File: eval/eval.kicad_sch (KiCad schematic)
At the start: 5 parts, among them J1 TC2030, U9 STM32G0B1CBTx

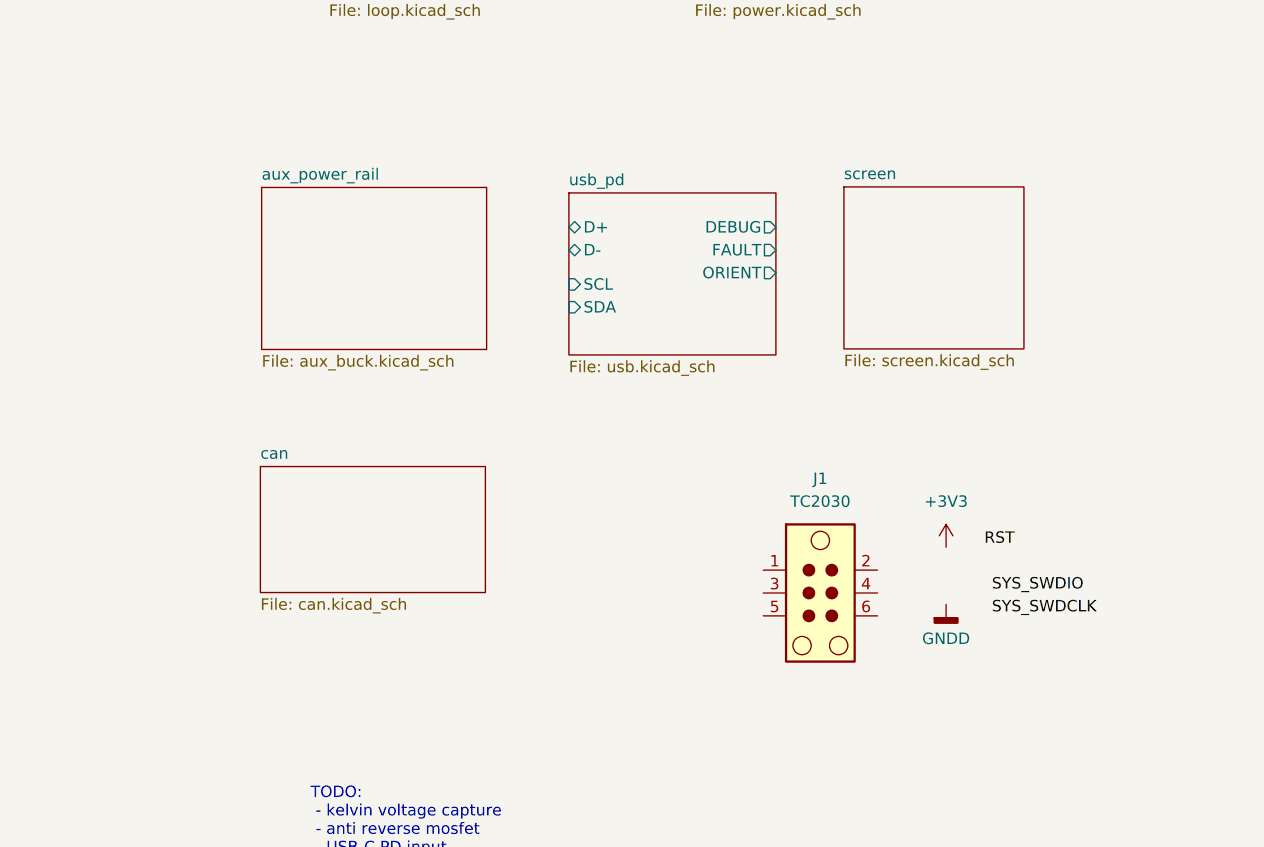
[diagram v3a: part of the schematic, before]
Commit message: add CAN to sch
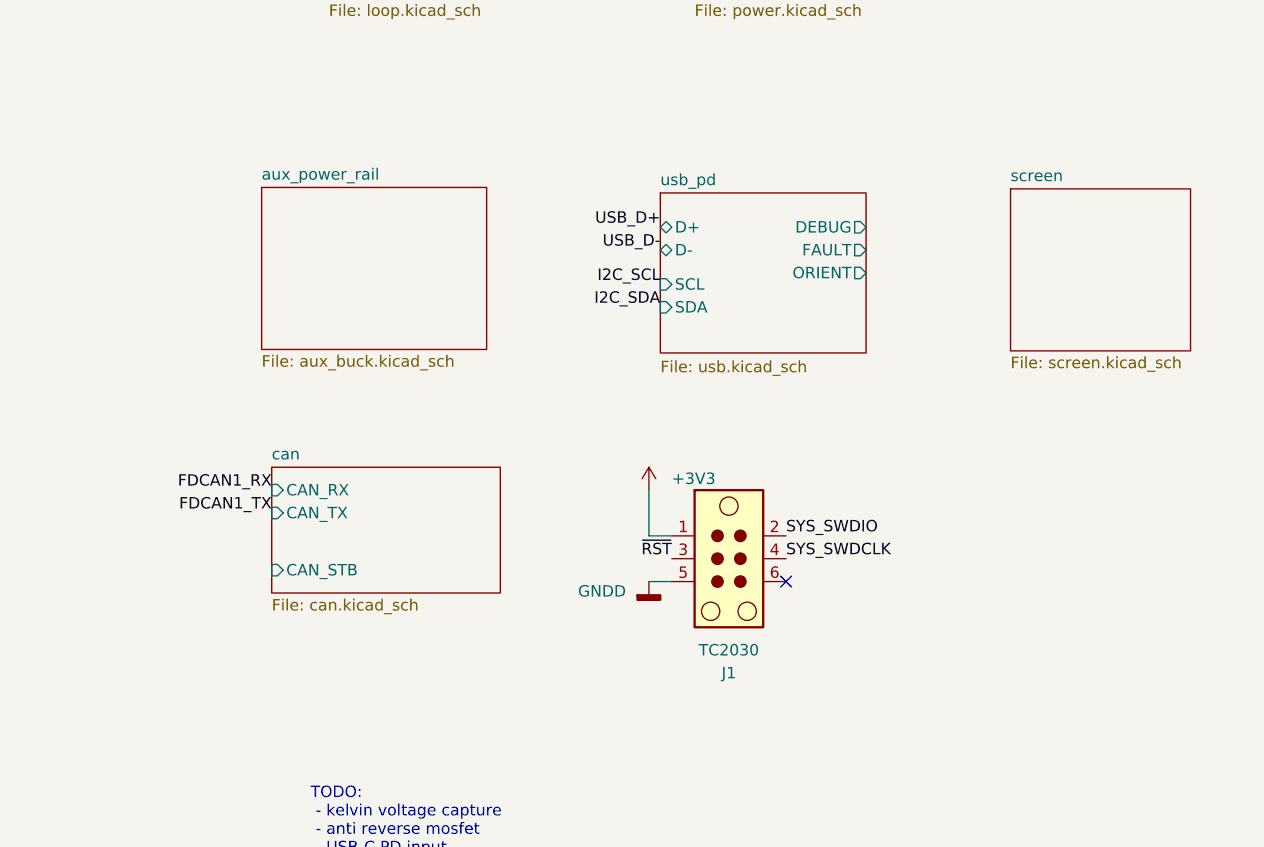
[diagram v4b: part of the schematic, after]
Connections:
- net +3V3: now also J1.1
- net GNDA: now also J1.5
- net SYS_SWDCLK: now also J1.4
- net SYS_SWDIO: now also J1.2
- net ~{RST}: now reaches J1.3
- no-connect marks 0 -> 1
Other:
- sheet can ports: added CAN_RX, CAN_STB, CAN_TX; removed none
- moved on the sheet: J1
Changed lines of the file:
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@@
 		(color 0 0 0 0)
 	)
+	(no_connect
+		(at 232.41 144.78)
+	)
 	(wire
 		(pts
@@
 	(wire
 		(pts
+			(xy 217.17 139.7) (xy 219.71 139.7)
+		)
+		(stroke
+			(width 0)
+			(type default)
+		)
+	)
+	(wire
+		(pts
 			(xy 34.29 59.69) (xy 52.07 59.69)
 		)
@@
 	(wire
 		(pts
+			(xy 217.17 134.62) (xy 217.17 139.7)
+		)
+		(stroke
+			(width 0)
+			(type default)
+		)
+	)
+	(wire
+		(pts
 			(xy 80.01 157.48) (xy 80.01 154.94)
 		)
@@
 		(pts
 			(xy 120.65 90.17) (xy 107.95 90.17)
+		)
+		(stroke
+			(width 0)
+			(type default)
+		)
+	)
+	(wire
+		(pts
+			(xy 217.17 144.78) (xy 219.71 144.78)
 		)
 		(stroke
@@
 		)
 	)
+	(label "FDCAN1_RX"
+		(at 175.26 134.62 180)
+		(effects
+			(font
+				(size 1.27 1.27)
+			)
+			(justify right bottom)
+		)
+	)
 	(label "UART1_TX"
 		(at 120.65 87.63 0)
@@
 		)
 	)
+	(label "I2C_SDA"
+		(at 218.44 114.3 180)
+		(effects
+			(font
+				(size 1.27 1.27)
+			)
+			(justify right bottom)
+		)
+	)
+	(label "FDCAN1_TX"
+		(at 175.26 137.16 180)
+		(effects
+			(font
+				(size 1.27 1.27)
+			)
+			(justify right bottom)
+		)
+	)
 	(label "BUCK_SYNC"
 		(at 259.08 63.5 0)
@@
 	)
 	(label "SYS_SWDCLK"
-		(at 255.27 148.59 0)
+		(at 232.41 142.24 0)
 		(effects
 			(font
@@
 		)
 	)
+	(label "USB_D+"
+		(at 218.44 105.41 180)
+		(effects
+			(font
+				(size 1.27 1.27)
+			)
+			(justify right bottom)
+		)
+	)
 	(label "I2C_SCL"
 		(at 107.95 110.49 0)
@@
 	)
 	(label "USB_D-"
+		(at 218.44 107.95 180)
+		(effects
+			(font
+				(size 1.27 1.27)
+			)
+			(justify right bottom)
+		)
+	)
+	(label "USB_D-"
 		(at 107.95 83.82 0)
 		(effects
@@
 		)
 	)
-	(label "RST"
-		(at 257.81 140.97 180)
+	(label "~{RST}"
+		(at 219.71 142.24 180)
 		(effects
 			(font
@@
 		)
 	)
+	(label "I2C_SCL"
+		(at 218.44 111.76 180)
+		(effects
+			(font
+				(size 1.27 1.27)
+			)
+			(justify right bottom)
+		)
+	)
 	(label "SPI2_MISO"
 		(at 107.95 138.43 0)
@@
 	)
 	(label "SYS_SWDIO"
-		(at 255.27 146.05 0)
+		(at 232.41 139.7 0)
 		(effects
 			(font
@@
 	(symbol
 		(lib_id "Connector:TC2030")
-		(at 234.95 146.05 0)
+		(at 224.79 142.24 0)
 		(unit 1)
 		(body_style 1)
@@
 		(fields_autoplaced yes)
 		(property "Reference" "J1"
-			(at 236.22 133.35 0)
+			(at 226.06 154.94 0)
 			(show_name no)
 			(do_not_autoplace no)
@@
 		)
 		(property "Value" "TC2030"
-			(at 236.22 135.89 0)
+			(at 226.06 152.4 0)
 			(show_name no)
 			(do_not_autoplace no)
@@
 		)
 		(property "Footprint" "Connector:Tag-Connect_TC2030-IDC-NL_2x03_P1.27mm_Vertical"
-			(at 236.22 146.05 0)
+			(at 226.06 142.24 0)
 			(hide yes)
 			(show_name no)
@@
 		)
 		(property "Datasheet" "https://www.tag-connect.com/wp-content/uploads/bsk-pdf-manager/2019/12/TC2030-IDC-NL-Datasheet-Rev-B.pdf"
-			(at 236.22 146.05 0)
+			(at 226.06 142.24 0)
 			(hide yes)
 			(show_name no)
@@
 		)
 		(property "Description" "Tag-Connect’s 6-pins connector"
-			(at 234.95 146.05 0)
+			(at 224.79 142.24 0)
 			(hide yes)
 			(show_name no)
@@
 	(symbol
 		(lib_id "power:GNDD")
-		(at 250.19 147.32 0)
+		(at 217.17 144.78 0)
 		(unit 1)
 		(body_style 1)
@@
 		(fields_autoplaced yes)
 		(property "Reference" "#PWR028"
-			(at 250.19 153.67 0)
+			(at 217.17 151.13 0)
 			(hide yes)
 			(show_name no)
@@
 		)
 		(property "Value" "GNDD"
-			(at 250.19 151.13 0)
-			(show_name no)
-			(do_not_autoplace no)
-			(effects
-				(font
-					(size 1.27 1.27)
-				)
+			(at 214.63 145.8596 0)
+			(show_name no)
+			(do_not_autoplace no)
+			(effects
+				(font
+					(size 1.27 1.27)
+				)
+				(justify right)
 			)
 		)
 		(property "Footprint" ""
-			(at 250.19 147.32 0)
+			(at 217.17 144.78 0)
 			(hide yes)
 			(show_name no)
@@
 		)
 		(property "Datasheet" ""
-			(at 250.19 147.32 0)
+			(at 217.17 144.78 0)
 			(hide yes)
 			(show_name no)
@@
 		)
 		(property "Description" "Power symbol creates a global label with name \"GNDD\" , digital ground"
-			(at 250.19 147.32 0)
+			(at 217.17 144.78 0)
 			(hide yes)
 			(show_name no)
@@
 	(symbol
 		(lib_id "power:+3V3")
-		(at 250.19 140.97 0)
+		(at 217.17 134.62 0)
 		(unit 1)
 		(body_style 1)
@@
 		(fields_autoplaced yes)
 		(property "Reference" "#PWR027"
-			(at 250.19 144.78 0)
+			(at 217.17 138.43 0)
 			(hide yes)
 			(show_name no)
@@
 		)
 		(property "Value" "+3V3"
-			(at 250.19 135.89 0)
-			(show_name no)
-			(do_not_autoplace no)
-			(effects
-				(font
-					(size 1.27 1.27)
-				)
+			(at 219.71 133.3499 0)
+			(show_name no)
+			(do_not_autoplace no)
+			(effects
+				(font
+					(size 1.27 1.27)
+				)
+				(justify left)
 			)
 		)
 		(property "Footprint" ""
-			(at 250.19 140.97 0)
+			(at 217.17 134.62 0)
 			(hide yes)
 			(show_name no)
@@
 		)
 		(property "Datasheet" ""
-			(at 250.19 140.97 0)
+			(at 217.17 134.62 0)
 			(hide yes)
 			(show_name no)
@@
 		)
 		(property "Description" "Power symbol creates a global label with name \"+3V3\""
-			(at 250.19 140.97 0)
+			(at 217.17 134.62 0)
 			(hide yes)
 			(show_name no)
@@
 	)
 	(sheet
-		(at 174 132)
-		(size 25 14)
+		(at 175.26 132.08)
+		(size 25.4 13.97)
 		(exclude_from_sim no)
 		(in_bom yes)
@@
 		)
 		(property "Sheetname" "can"
-			(at 174 131.2884 0)
+			(at 175.26 131.3684 0)
 			(show_name no)
 			(do_not_autoplace no)
@@
 		)
 		(property "Sheetfile" "can.kicad_sch"
-			(at 174 146.5846 0)
+			(at 175.26 146.6646 0)
 			(show_name no)
 			(do_not_autoplace no)
@@
 				)
 				(justify left top)
+			)
+		)
+		(pin "CAN_RX" input
+			(at 175.26 134.62 180)
+			(effects
+				(font
+					(size 1.27 1.27)
+				)
+				(justify left)
+			)
+		)
+		(pin "CAN_STB" input
+			(at 175.26 143.51 180)
+			(effects
+				(font
+					(size 1.27 1.27)
+				)
+				(justify left)
+			)
+		)
+		(pin "CAN_TX" input
+			(at 175.26 137.16 180)
+			(effects
+				(font
+					(size 1.27 1.27)
+				)
+				(justify left)
 			)
 		)
@@
 	)
 	(sheet
-		(at 208.28 101.6)
-		(size 23 18)
+		(at 218.44 101.6)
+		(size 22.86 17.78)
 		(exclude_from_sim no)
 		(in_bom yes)
@@
 		)
 		(property "Sheetname" "usb_pd"
-			(at 208.28 100.8884 0)
+			(at 218.44 100.8884 0)
 			(show_name no)
 			(do_not_autoplace no)
@@
 		)
 		(property "Sheetfile" "usb.kicad_sch"
-			(at 208.28 120.1846 0)
+			(at 218.44 120.1846 0)
 			(show_name no)
 			(do_not_autoplace no)
@@
 		)
 		(pin "D+" bidirectional
-			(at 208.28 105.41 180)
+			(at 218.44 105.41 180)
 			(effects
 				(font
@@
 		)
 		(pin "D-" bidirectional
-			(at 208.28 107.95 180)
+			(at 218.44 107.95 180)
 			(effects
 				(font
@@
 		)
 		(pin "DEBUG" output
-			(at 231.28 105.41 0)
+			(at 241.3 105.41 0)
 			(effects
 				(font
@@
 		)
 		(pin "FAULT" output
-			(at 231.28 107.95 0)
+			(at 241.3 107.95 0)
 			(effects
 				(font
@@
 		)
 		(pin "ORIENT" output
-			(at 231.28 110.49 0)
+			(at 241.3 110.49 0)
 			(effects
 				(font
@@
 		)
 		(pin "SCL" input
-			(at 208.28 111.76 180)
+			(at 218.44 111.76 180)
 			(effects
 				(font
@@
 		)
 		(pin "SDA" input
-			(at 208.28 114.3 180)
+			(at 218.44 114.3 180)
 			(effects
 				(font
@@
 	)
 	(sheet
-		(at 238.84 100.93)
+		(at 257.35 101.15)
 		(size 20 18)
 		(exclude_from_sim no)
@@
 		)
 		(property "Sheetname" "screen"
-			(at 238.84 100.2184 0)
+			(at 257.35 100.4384 0)
 			(show_name no)
 			(do_not_autoplace no)
@@
 		)
 		(property "Sheetfile" "screen.kicad_sch"
-			(at 238.84 119.5146 0)
-			(show_name no)
-			(do_not_autoplace no)
+			(at 257.35 119.7346 0)
+			(show_name no)
+			(do_not_autoplace no)

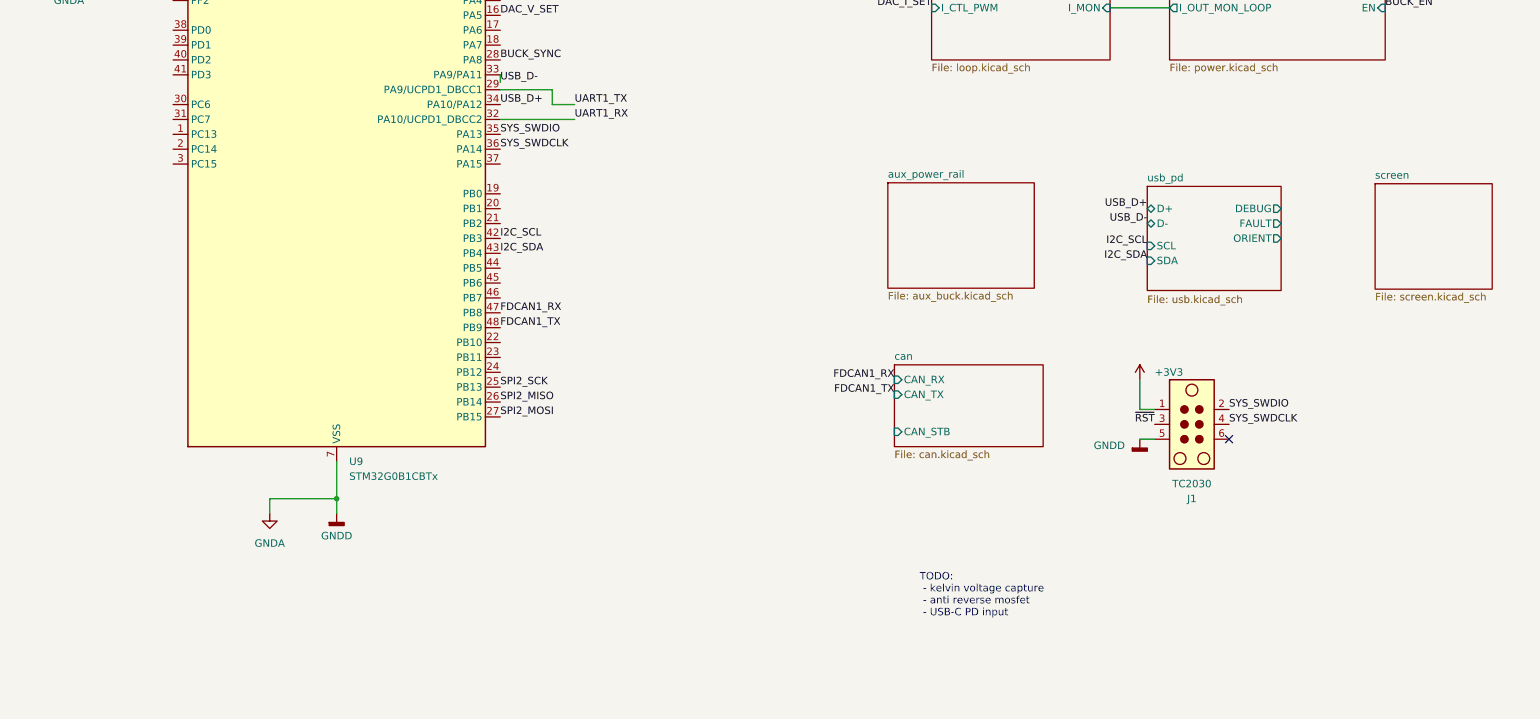
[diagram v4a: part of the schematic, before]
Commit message: [Layout] complete loop, root and buck layout
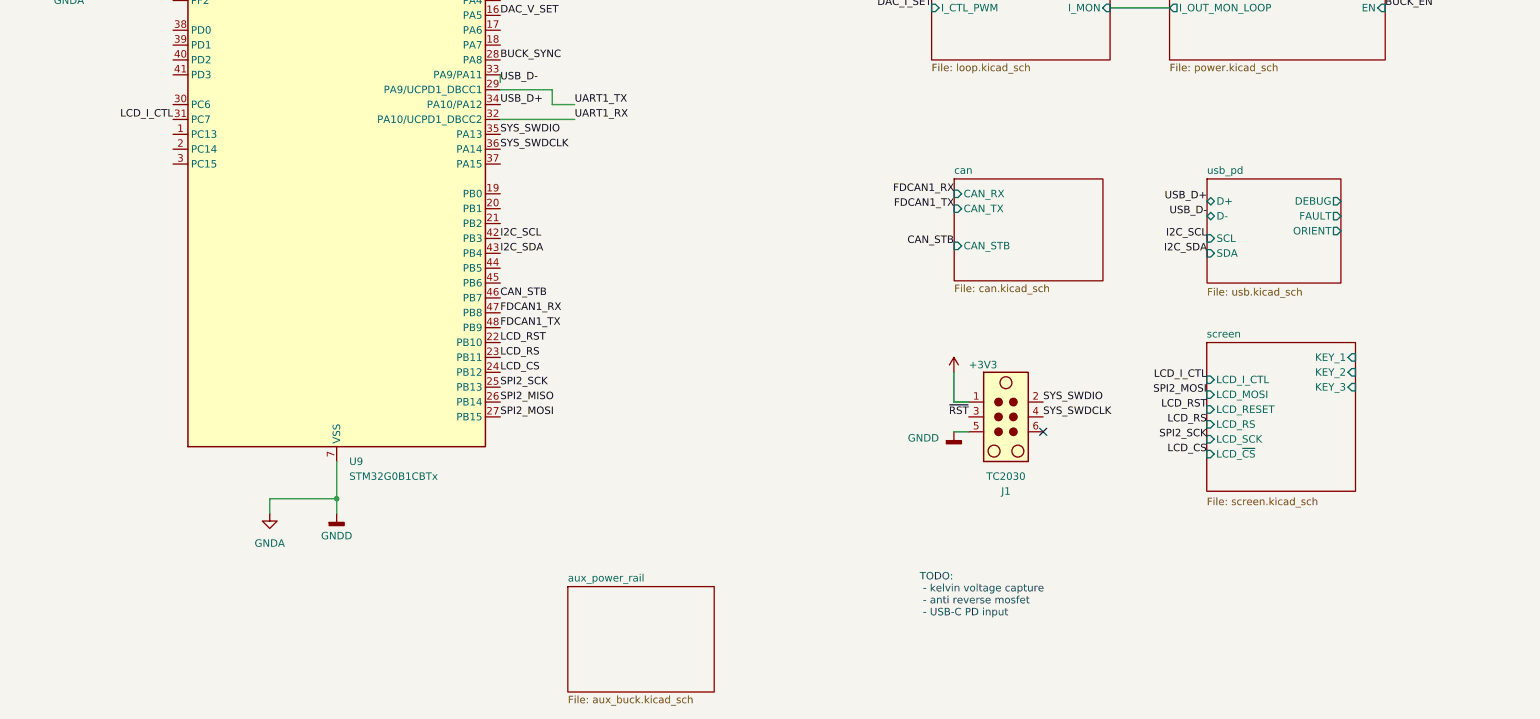
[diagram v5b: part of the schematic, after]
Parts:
- C19, C20, C21: footprint (none) -> Capacitor_SMD:C_0603_1608Metric
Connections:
- net LCD_RST: now reaches U9.22 (PB10)
- net LCD_RS: now reaches U9.23 (PB11)
- net LCD_CS: now reaches U9.24 (PB12)
- net LCD_I_CTL: now reaches U9.31 (PC7)
- net CAN_STB: now reaches U9.46 (PB7)
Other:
- sheet screen ports: added KEY_1, KEY_2, KEY_3, LCD_I_CTL, LCD_MOSI, LCD_RESET, LCD_RS, LCD_SCK, LCD_~{CS}; removed none
- moved on the sheet: J1

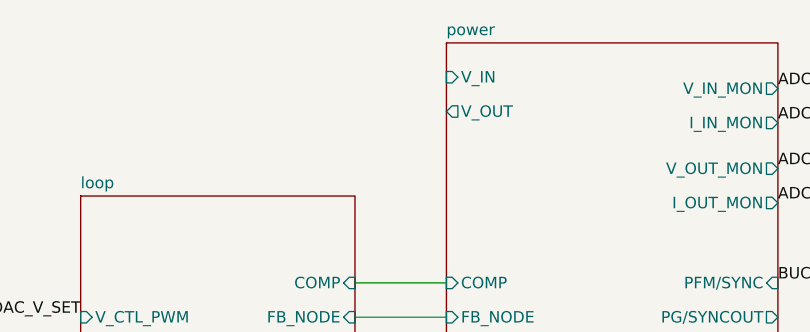
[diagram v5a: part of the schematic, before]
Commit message: [layout] trying to put all components in limit dimention
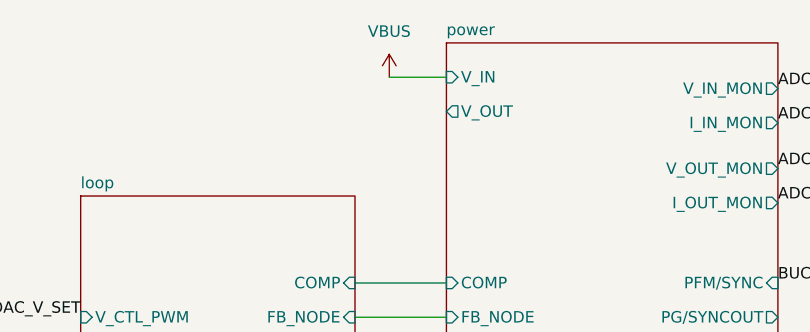
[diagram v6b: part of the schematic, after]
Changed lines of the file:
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@@
+	(wire
+		(pts
+			(xy 215.9 40.64) (xy 222.25 40.64)
+		)
+		(stroke
+			(width 0)
+			(type default)
+		)
+	)
 	(wire
 		(pts
@@
 					(unit 1)
 				)
+			)
+		)
+	)
+	(symbol
+		(lib_id "power:VBUS")
+		(at 215.9 40.64 0)
+		(unit 1)
+		(body_style 1)
+		(exclude_from_sim no)
+		(in_bom yes)
+		(on_board yes)
+		(in_pos_files yes)
+		(dnp no)
+		(fields_autoplaced yes)
+		(property "Reference" "#PWR083"
+			(at 215.9 44.45 0)
+			(hide yes)
+			(show_name no)
+			(do_not_autoplace no)
+			(effects
+				(font
+					(size 1.27 1.27)
+				)
+			)
+		)
+		(property "Value" "VBUS"
+			(at 215.9 35.56 0)
+			(show_name no)
+			(do_not_autoplace no)
+			(effects
+				(font
+					(size 1.27 1.27)
+				)
+			)
+		)
+		(property "Footprint" ""
+			(at 215.9 40.64 0)
+			(hide yes)
+			(show_name no)
+			(do_not_autoplace no)
+			(effects
+				(font
+					(size 1.27 1.27)
+				)
+			)
+		)
+		(property "Datasheet" ""
+			(at 215.9 40.64 0)
+			(hide yes)
+			(show_name no)
+			(do_not_autoplace no)
+			(effects
+				(font
+					(size 1.27 1.27)
+				)
+			)
+		)
+		(property "Description" "Power symbol creates a global label with name \"VBUS\""
+			(at 215.9 40.64 0)
+			(hide yes)
+			(show_name no)
+			(do_not_autoplace no)
+			(effects
+				(font
+					(size 1.27 1.27)
+				)
+			)
+		)
+		(pin "1"
+		)
+		(instances
+			(project "eval"
+				(path "/8b023652-20db-48ce-ad53-bc2d9a4e5dd4"
+					(reference "#PWR083")
+					(unit 1)
+				)
